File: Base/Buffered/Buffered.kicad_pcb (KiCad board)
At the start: 2 copper layers, 30 x 84 mm, 50 parts, among them J1 Barrel_Jack_Switch, J2 Conn_01x04_Pin, J3 Conn_01x04_Pin, J4 AudioJack2_Ground, J5 AudioJack2_Ground, Q1 DMC3071LVT, Q2 40V, Q3 LS844, SW1 SW_Push, U1 LT3462A

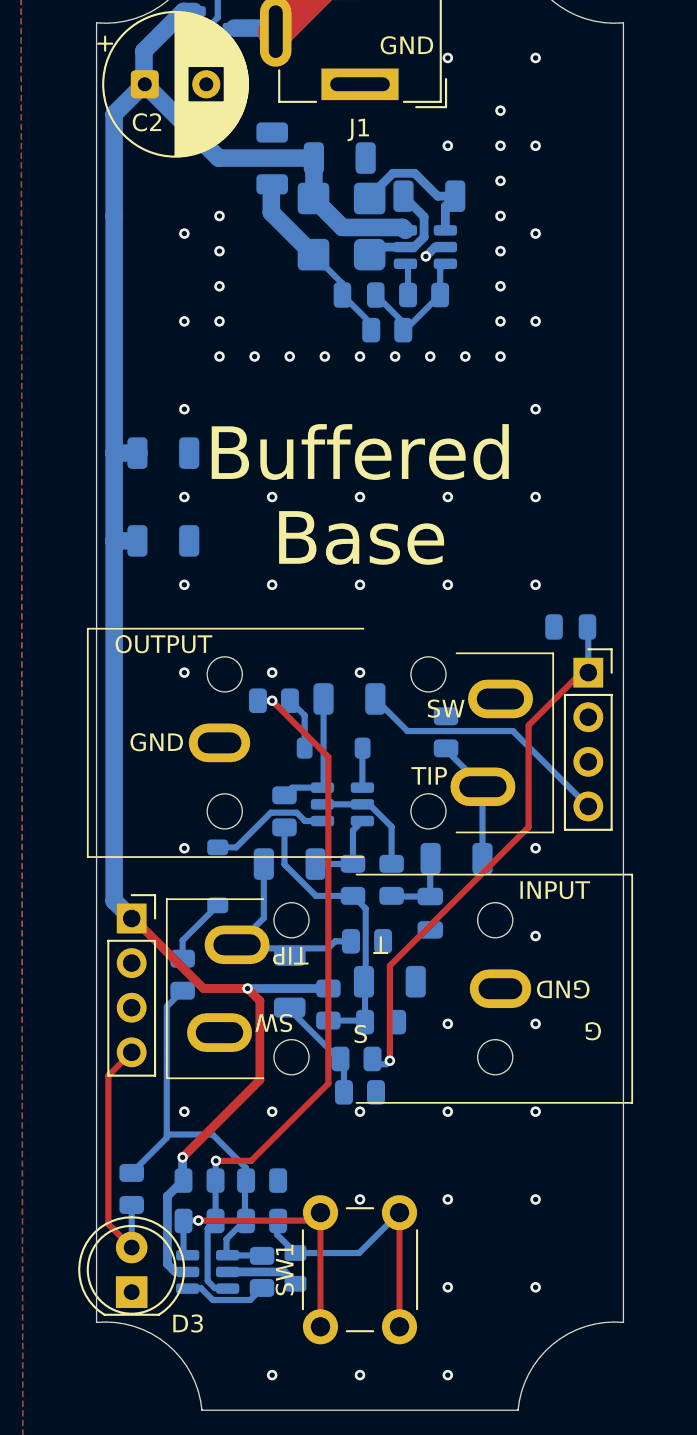
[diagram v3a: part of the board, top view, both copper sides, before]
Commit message: Buffered base: use negative rail for JFET switching
This _still_ doesn't do any actual buffering, but with the negative
rail, we now no longer need to rebase the signals to some mid-point
voltage, and we can just leave the signals ground-references and use the
negative rail for switching.

That streamlines the signal path, and will make it easier to just insert
an opamp or two in there too.  But I remain more interested in getting
the switching side sorted out properly, so that's the primary goal here.

This tweaks the push-on push-off circuit a bit too, since taht one now
needs to switch between positive and negative voltages rather than VIN
and ground.

Signed-off-by: Linus Torvalds <torvalds@linux-foundation.org>
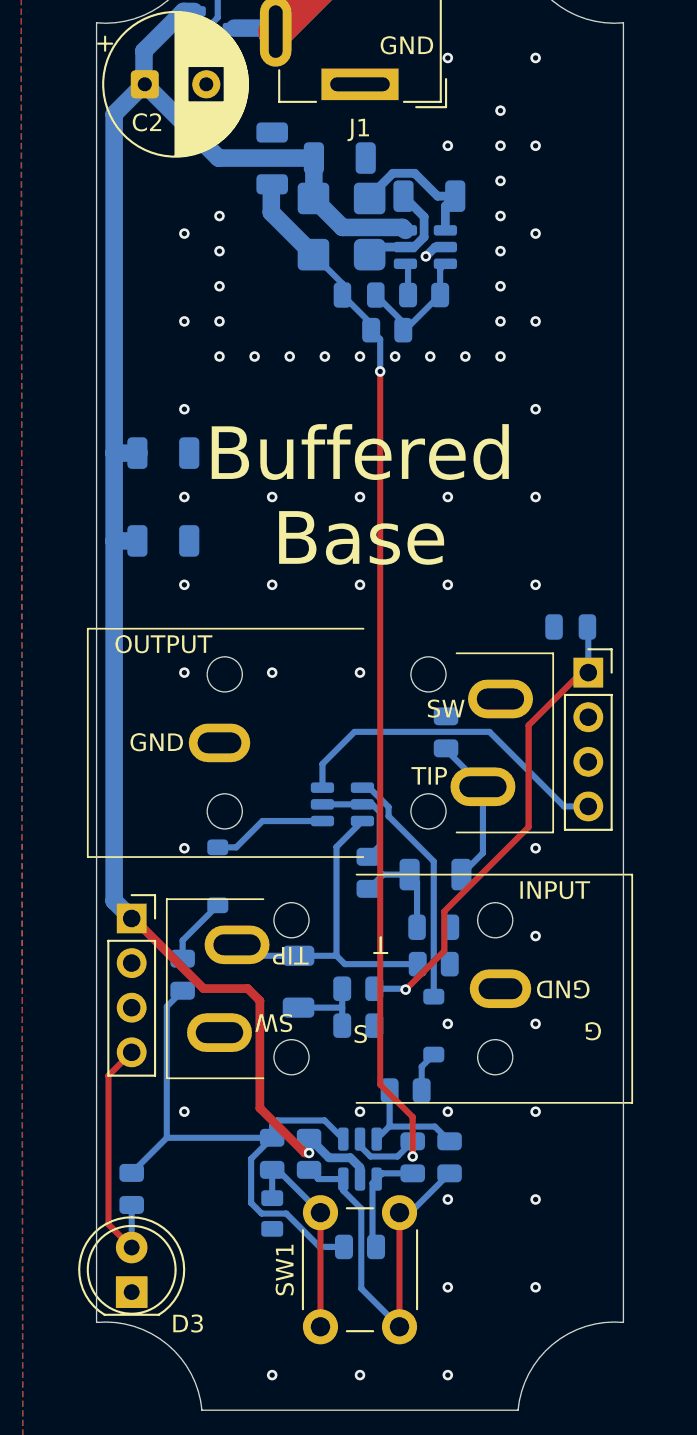
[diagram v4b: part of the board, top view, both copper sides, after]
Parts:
- removed C10, C5, C6: 1uF, Capacitor_SMD:C_1206_3216Metric
- removed R14, R3, R5: 22k, Resistor_SMD:R_0805_2012Metric
- removed R15: 47k, Resistor_SMD:R_0805_2012Metric
- R16, R17: value 22k -> 100k
- R8, R9: value 1MEG -> 22k
- moved R8 25.2 mm to (100.0, 132.7), turned to 180 degrees
- moved R16 23.4 mm to (102.6, 123.8)
- moved D1 16.8 mm to (104.2, 120.1), turned to 90 degrees
- moved R9 16.7 mm to (105.1, 127.6)
- moved Q1 10.8 mm to (100.0, 127.7), turned to 90 degrees
- moved R7 8.68 mm to (103.0, 127.6), turned to -90 degrees
- moved R2 6.42 mm to (97.1, 127.4), turned to 90 degrees
- moved R10 4.02 mm to (104.2, 116.6)
- moved R12 4.00 mm to (99.9, 118.0)
- moved R6 3.87 mm to (95.0, 127.4), turned to 90 degrees
- moved R11 3.80 mm to (99.9, 120.1)
- moved C1 3.39 mm to (95.0, 130.8)
- moved C9 1.50 mm to (104.3, 111.5)
- moved R23 1.36 mm to (100.5, 111.4)
- moved C11 0.82 mm to (104.2, 114.5), turned to 0 degrees
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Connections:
- Q1 pad 5: GND -> -V
- Q3 pad 3: Net-(Q3A-S) -> OUT^{EFF}
- Q3 pad 6: Net-(Q3B-S) -> IN^{CONN}
- R2 pad 1: ON_LOW -> SW1
- R7 pad 1: GND -> -V
- R7 pad 2: ON_HIGH -> Net-(Q1A-G)
- R8 pad 1: MIDBIAS -> Net-(Q1A-G)
- R8 pad 2: Net-(Q3A-S) -> ON_HIGH
- R9 pad 1: Net-(Q3B-S) -> ON_LOW
- R9 pad 2: MIDBIAS -> SW1
- SW1 pad 1: SW1 -> SW2
- SW1 pad 2: SW2 -> SW1
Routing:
- net -V: track 10.7 -> 63.5 mm, vias 0 -> 2
- net ON_LOW: track 40.5 -> 6.85 mm, vias 2 -> 0
- net MIDBIAS: track 16.4 -> 0.00 mm
- net GATE^{OFF}: track 2.26 -> 13.8 mm
- net ON_HIGH: track 24.4 -> 33.4 mm
- net VIN: track 109.1 -> 101.1 mm, vias 2 -> 1
- net Net-(Q3A-S): track 7.42 -> 0.00 mm
- net IN^{CONN}: track 12.0 -> 19.0 mm
- net SW1: track 16.5 -> 22.2 mm, vias 1 -> 0
- net Net-(Q3B-S): track 4.79 -> 0.00 mm
- net OUT^{EFF}: track 14.7 -> 19.0 mm
- net GND: track 5.47 -> 1.33 mm, vias 63 -> 61
- net IN^{EFF}: track 30.9 -> 27.0 mm
- net SW2: track 15.7 -> 11.9 mm
- net Net-(C7-Pad2): track 6.16 -> 4.60 mm
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
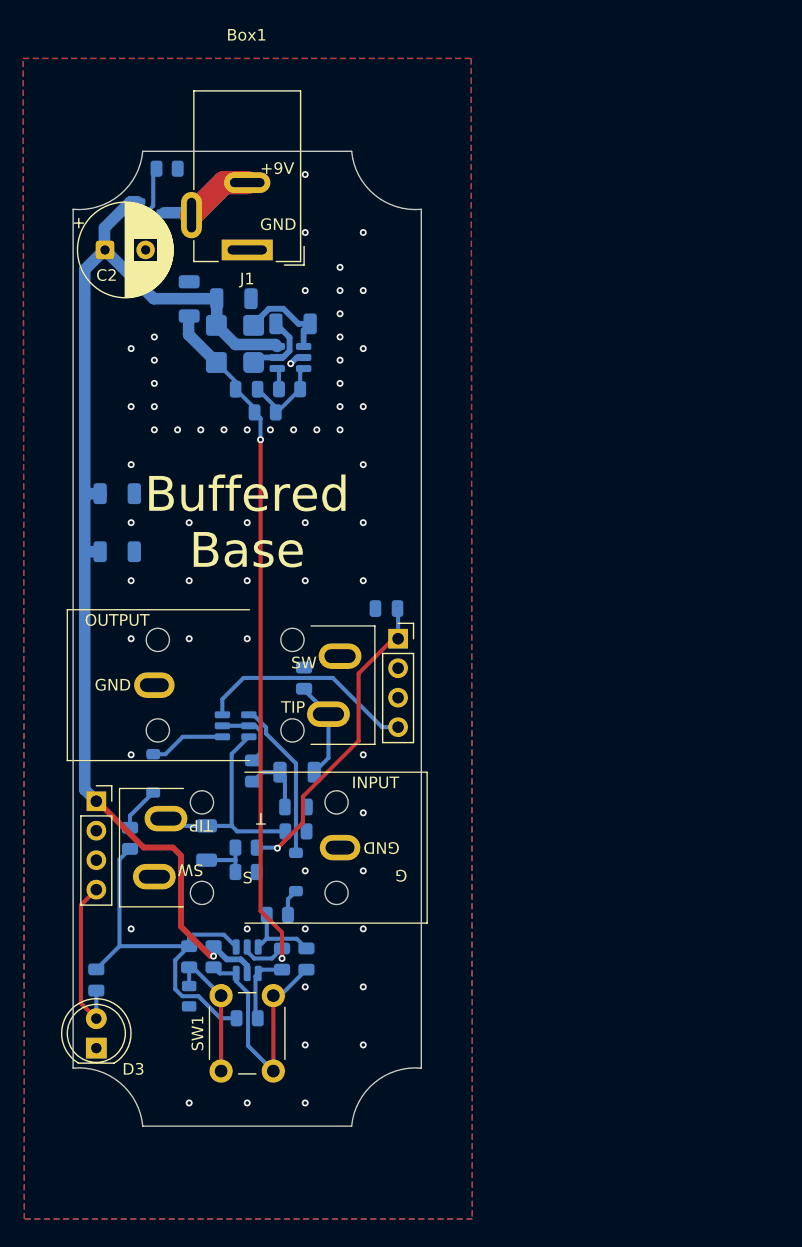
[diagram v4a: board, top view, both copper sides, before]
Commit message: Update the buffered base board
The JFET switching worked fine, but since this all started as an
exercise in using MOSFETs, let's just go all in on that, and use the
MOSFETs for switching the signal too.

Due to the body diode, you need two MOSFETs in series for the signal
switching, so it's four MOSFETs instead of two JFETs, but despite that
the end result is actually simpler.  And those dual MOSFET things are
common and dirt cheap, unlike the special matched JFET package.

Since I can just continue to use the dual complementary MOSFETs, I can
use PMOS for one signal and NMOS for the other, and share all the gate
circuit.  Plus no need for a diode to protect the gate current messing
with the signal.

Also update the resistor value in the switching circuit and make the
time constant be 100ms.  That seems to make it more reliable in testing,
although I'm not convinced my testing with the original value was all
that great.  The soft-switch circuit does seem to work, though.

Also, since the LED pin on the board connectors has never been used,
let's just re-purpose that as a negative voltage pin for the effect
board.  If some effect board wants to touch the LED status, it might as
well just connect to the LED itself.  Having access to a dual voltage
rail would seem to be a lot more important.

Finally - and probably most importantly for actual sound and current
effects boards - add a low-pass filter on the voltage lines.  Because as
expected, the negative power supply did add a lot of noise to the VIN
line.

The base board itself doesn't actually care, but the effects boards do.

An actual LDO would be better, but I don't have any simple fixed ones in
my parts library (except for the 5V one, which seems a bit sad).
Current effects boards don't use a lot of current and only care about
the voltage being stable, so let's try this simple model.

Signed-off-by: Linus Torvalds <torvalds@linux-foundation.org>
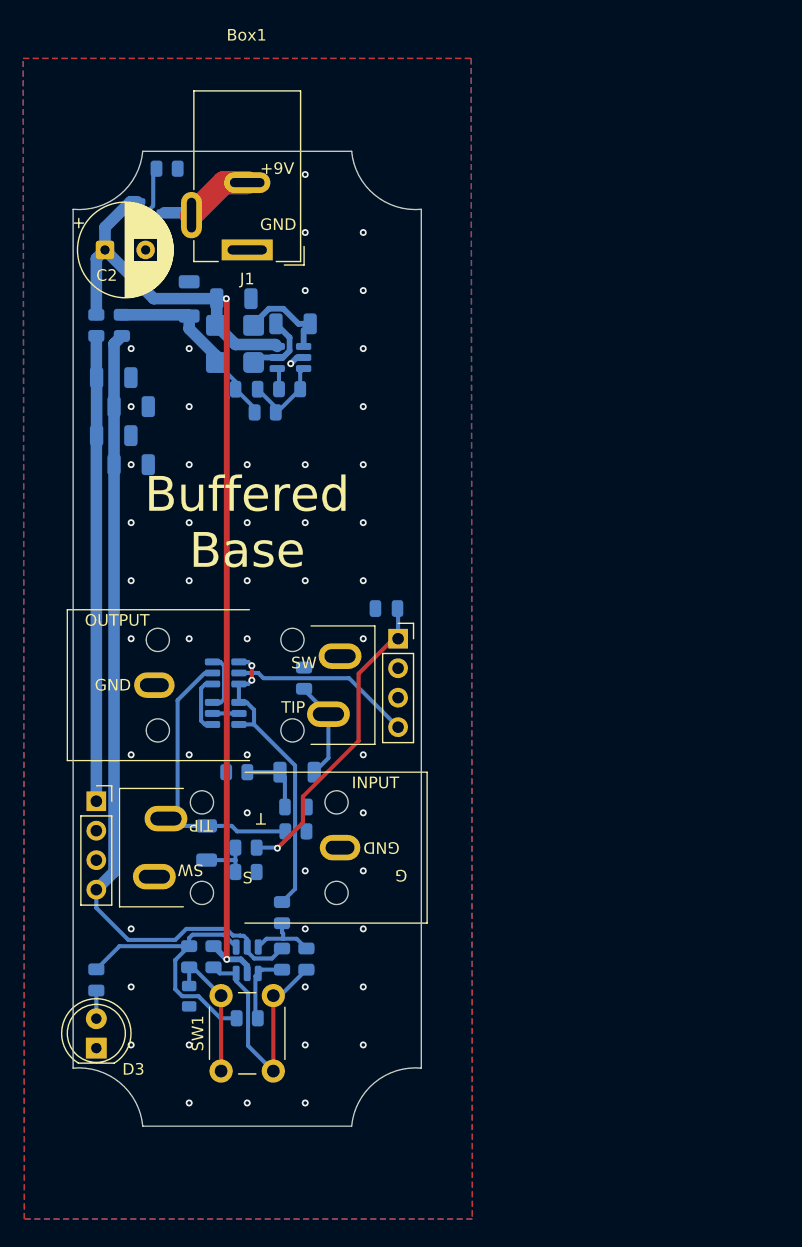
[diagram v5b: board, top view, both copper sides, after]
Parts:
- removed C3: 10uF, Capacitor_SMD:C_1206_3216Metric
- removed C4: 1uF, Capacitor_SMD:C_1206_3216Metric
- removed D1, D2: BAT41Z, Diode_SMD:D_SOD-123
- removed R16, R17: 100k, Resistor_SMD:R_0805_2012Metric
- added C10: 10uF, Capacitor_SMD:C_1206_3216Metric, B.Cu at (88.5, 82.5)
- added C16: 10uF, Capacitor_SMD:C_1206_3216Metric, B.Cu at (90.0, 85.0)
- added C5: 47uF, Capacitor_SMD:C_1206_3216Metric, B.Cu at (88.5, 77.5)
- added C6: 47uF, Capacitor_SMD:C_1206_3216Metric, B.Cu at (90.0, 80.0)
- added Q4: DMC3071LVT, Package_TO_SOT_SMD:TSOT-23-6, B.Cu at (98.2, 106.4)
- added R14: 220R, Resistor_SMD:R_0805_2012Metric, B.Cu at (89.2, 73.0)
- added R3: 10MEG, Resistor_SMD:R_0805_2012Metric, B.Cu at (103.0, 123.6)
- added R5: 220R, Resistor_SMD:R_0805_2012Metric, B.Cu at (87.0, 73.0)
- Q3: value LS844 -> DMC3071LVT; footprint Package_TO_SOT_SMD:SOT-23-6 -> Package_TO_SOT_SMD:TSOT-23-6
- R6: value 220k -> 1MEG
- moved Q3 4.63 mm to (98.2, 103.0), turned to 180 degrees
- moved R23 1.40 mm to (99.1, 111.5), turned to 0 degrees
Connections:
- C13 pad 2: -V -> VNEG
- C15 pad 1: -V -> VNEG
- J3 pad 1: VIN -> +V
- J3 pad 4: LED -> -V
- L1 pad 2: -V -> VNEG
- Q3 pad 1: GATE^{ON} -> Net-(Q3A-G)
- Q3 pad 2: Net-(Q3A-D) -> OUT^{EFF}
- Q3 pad 3: OUT^{EFF} -> Net-(Q3A-G)
- Q3 pad 4: GATE^{OFF} -> Net-(Q3B-D)
- Q3 pad 5: Net-(Q3A-D) -> IN^{CONN}
- Q3 pad 6: IN^{CONN} -> Net-(Q3A-D)
- R23 pad 1: Net-(Q3A-D) -> Net-(Q4A-S)
- R24 pad 1: -V -> VNEG
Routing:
- net +V: track 0.00 -> 40.1 mm
- net Net-(Q3A-G): track 0.00 -> 26.7 mm, vias 0 -> 2
- net VNEG: track 0.00 -> 16.5 mm
- net GATE^{OFF}: track 13.8 -> 0.00 mm
- net LED: track 14.6 -> 2.42 mm
- net ON_HIGH: track 33.4 -> 24.7 mm
- net VIN: track 101.1 -> 93.3 mm, vias 1 -> 2
- net Net-(Q4A-S): track 0.00 -> 7.33 mm
- net GATE^{ON}: track 6.58 -> 0.00 mm
- net -V: track 63.5 -> 69.8 mm, vias 2 -> 0
- net IN^{CONN}: track 19.0 -> 24.7 mm
- net Net-(Q3B-D): track 0.00 -> 5.05 mm
- net Net-(D2-K): track 3.87 -> 0.00 mm
- net OUT^{EFF}: track 19.0 -> 15.6 mm
- net Net-(D1-K): track 2.33 -> 0.00 mm
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
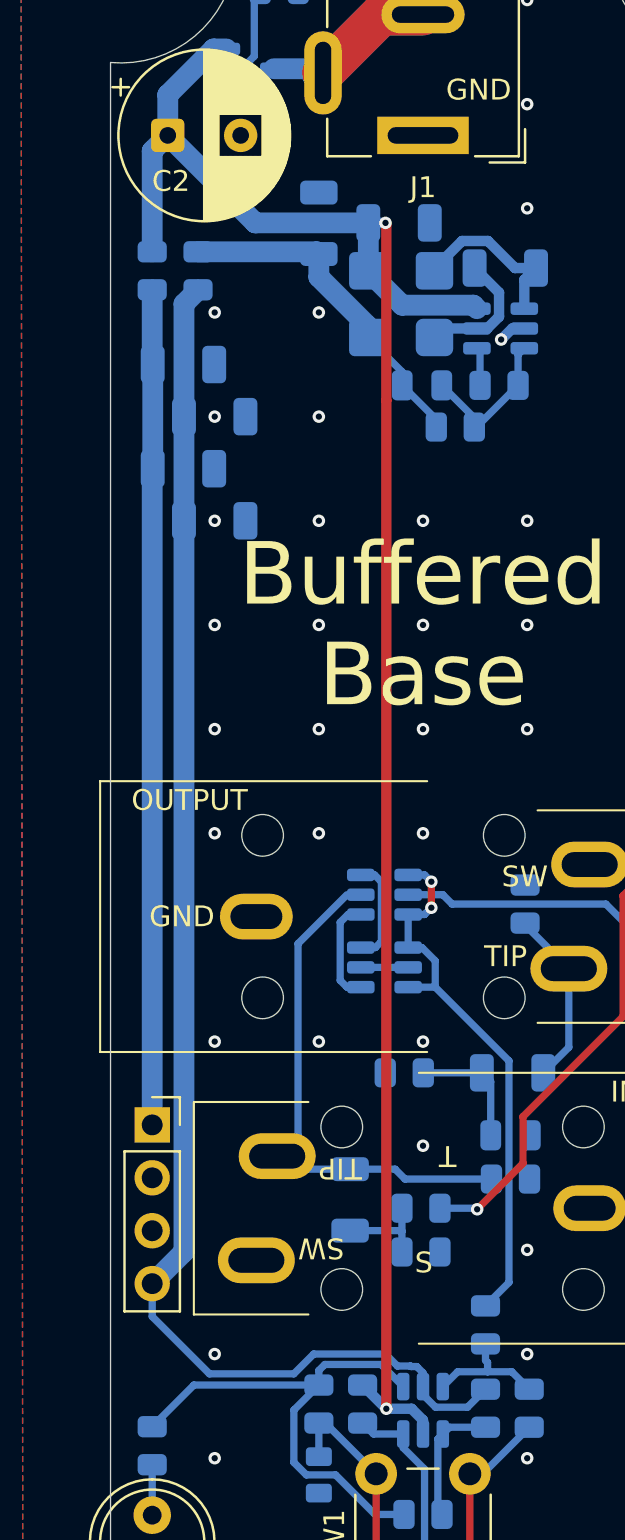
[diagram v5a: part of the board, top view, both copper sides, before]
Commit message: Try LDO for positive voltage rail cleaning
As mentioned, I don't think I'll actually build this, because it seems
pointlessly complicated.  But I did the basic design and layout for it
just in case.

I think I'll go back to the single-rail design and keep the MOSFET
switching.

I also think I need to come up with a new project.  I'm kind of running
out of ideas of small projects to do that I can build and test.  I like
the switching circuit, but I'm losing interest in the effects board side
since I still can't actually play guitar.

Signed-off-by: Linus Torvalds <torvalds@linux-foundation.org>
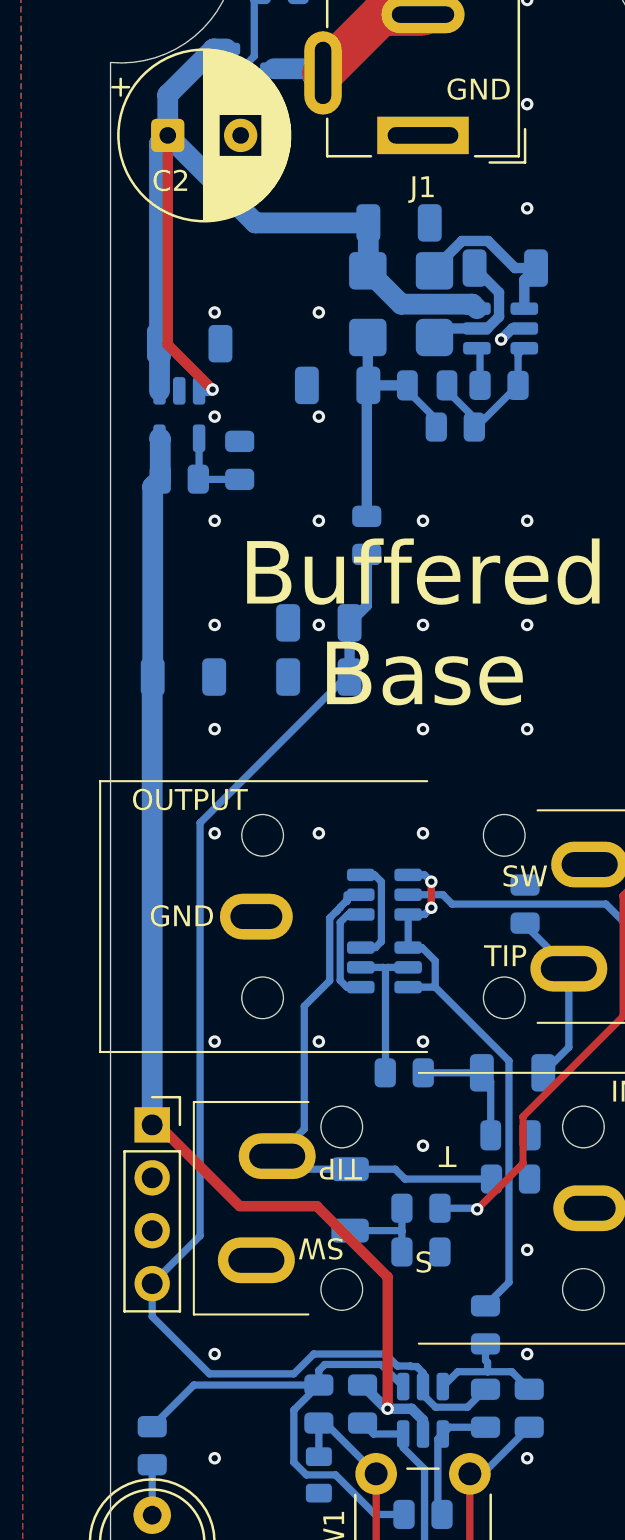
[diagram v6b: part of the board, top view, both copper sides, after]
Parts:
- removed C10: 10uF, Capacitor_SMD:C_1206_3216Metric
- removed C5: 47uF, Capacitor_SMD:C_1206_3216Metric
- removed R5: 220R, Resistor_SMD:R_0805_2012Metric
- added C3: 10uF, Capacitor_SMD:C_1206_3216Metric, B.Cu at (88.5, 92.5)
- added C4: 10uF, Capacitor_SMD:C_1206_3216Metric, B.Cu at (88.8, 76.5)
- added R15: 10k, Resistor_SMD:R_0805_2012Metric, B.Cu at (88.3, 83.0)
- added R16: 54k, Resistor_SMD:R_0805_2012Metric, B.Cu at (91.2, 82.1)
- added U2: AP2202-ADJ, Package_TO_SOT_SMD:SOT-23-5, B.Cu at (88.3, 79.9)
- R25: value 37.5k -> 42k2
- moved R14 15.1 mm to (97.3, 85.7)
- moved C6 11.1 mm to (95.0, 89.9), turned to 180 degrees
- moved C16 9.01 mm to (95.0, 92.5), turned to 180 degrees
- moved C15 7.83 mm to (95.9, 78.5), turned to 180 degrees
- moved C13 0.25 mm to (100.2, 78.5)
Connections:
- Q1 pad 2: VIN -> +V
- R2 pad 2: VIN -> +V
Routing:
- net VIN: track 93.3 -> 51.5 mm, vias 2 -> 1
- net +V: track 40.1 -> 58.0 mm, vias 0 -> 1
- net -V: track 69.8 -> 60.5 mm
- net Net-(U2-ADJ): track 0.00 -> 3.97 mm
- net VNEG: track 16.5 -> 12.8 mm
- net GND: vias 52 -> 51
